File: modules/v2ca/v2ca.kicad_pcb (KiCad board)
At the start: 2 copper layers, 30.5 x 68.6 mm, 24 parts, among them U1 VTL5C, U2 MCP6002-xSN, U3 VTL5C, U4 MCP6002-xSN, U5 MCP6002-xSN

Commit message: v2ca_1.0.0
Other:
- board text added: "V2CA 1.0.0"
- board text removed: "V2CA 0.1.0"
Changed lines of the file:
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@@
 		)
 	)
-	(gr_text "V2CA\n0.1.0"
+	(gr_text "V2CA\n1.0.0"
 		(at 76.073 107.95 0)
 		(layer "F.SilkS")

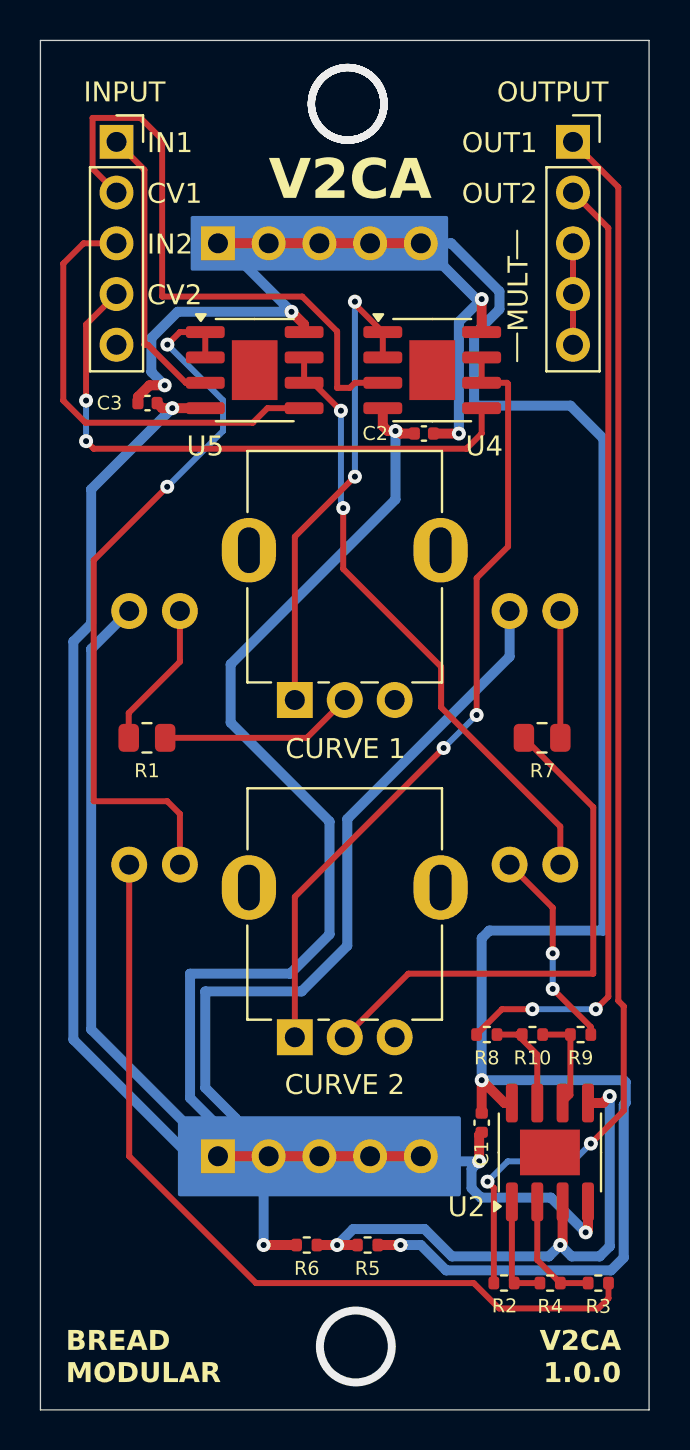
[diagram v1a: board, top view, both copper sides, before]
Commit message: v2ca: update footprints of pots
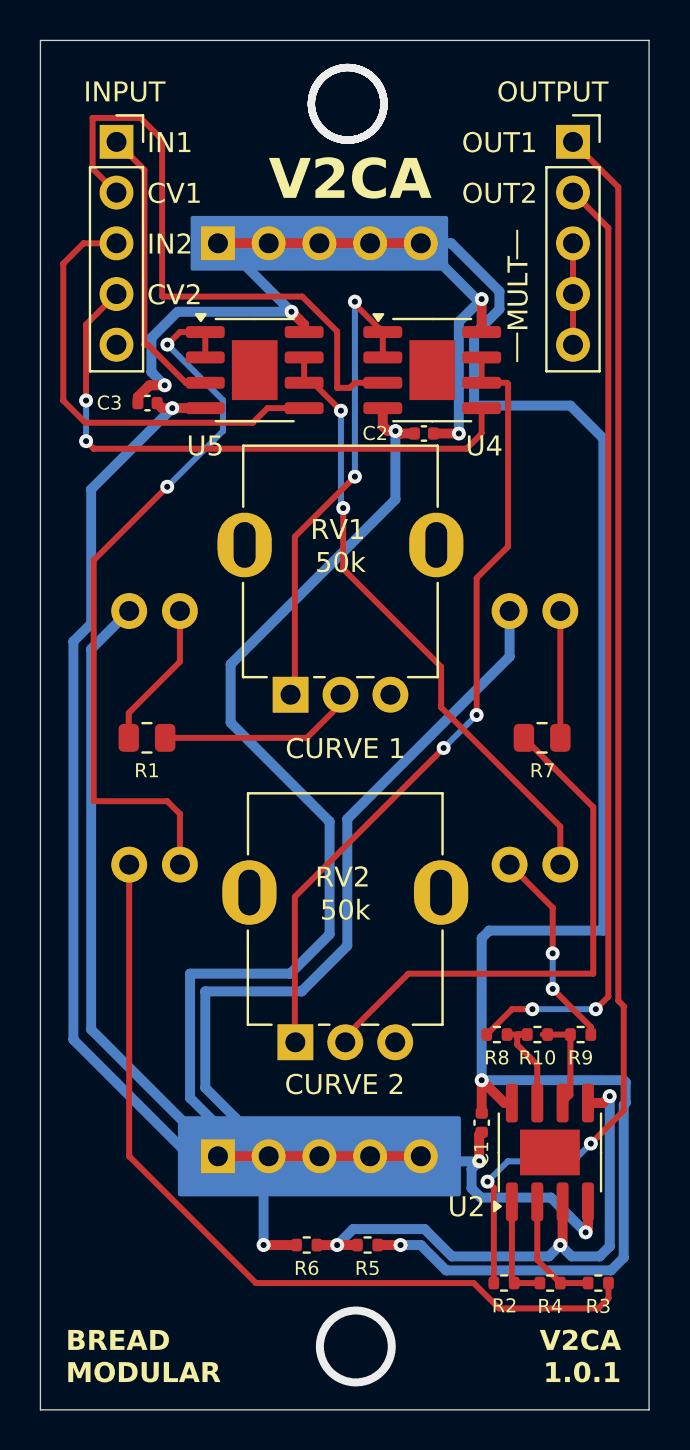
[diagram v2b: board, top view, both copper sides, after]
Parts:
- moved RV1 7.65 mm to (62.1, 66.4), turned to 0 degrees
- moved RV2 7.24 mm to (62.4, 83.8), turned to 0 degrees
- moved R8 0.51 mm to (69.8, 90.4)
- moved R10 0.25 mm to (71.9, 90.4)
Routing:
- net V2_OUT: track 48.4 -> 47.9 mm
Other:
- board text added: "V2CA 1.0.1"
- board text removed: "V2CA 1.0.0"
